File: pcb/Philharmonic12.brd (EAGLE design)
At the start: 97.8 x 95.2 mm, 47 parts, among them IC1 MC68B21, IC10 74LS74N, IC2 AY-3-8910-RP, IC3 AY-3-8910-RP, IC4 AY-3-8910-RP, IC5 AY-3-8910-RP, IC6 74LS138N, IC7 74LS30N, IC8 LM386N-1, IC9 LM386N-1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

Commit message: Small dimension updates
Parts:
- IC2, IC3, IC4, IC5: value AY-3-8910-RP -> AY-3-8910
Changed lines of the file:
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@@
 www.go4retro.com
 CC-BY-SA 4.0</text>
+<dimension x1="-25.4" y1="0" x2="-25.4" y2="95.25" x3="-55.88" y3="47.625" textsize="1.778" layer="48"/>
+<dimension x1="-48.895" y1="93.98" x2="48.895" y2="93.98" x3="0" y3="97.79" textsize="1.778" layer="48"/>
 </plain>
 <attributes>
@@
 <attribute name="VALUE" x="0" y="29.21" size="1.778" layer="27" align="bottom-center"/>
 </element>
-<element name="IC2" library="general-instrument" package="DIL40-RP" value="AY-3-8910-RP" x="-39.37" y="68.58" smashed="yes" rot="R90">
+<element name="IC2" library="general-instrument" package="DIL40-RP" value="AY-3-8910" x="-39.37" y="68.58" smashed="yes" rot="R90">
 <attribute name="NAME" x="-47.625" y="41.91" size="1.778" layer="25" ratio="10"/>
 <attribute name="VALUE" x="-38.735" y="68.58" size="1.778" layer="27" ratio="10" rot="R90" align="bottom-center"/>
 </element>
-<element name="IC3" library="general-instrument" package="DIL40-RP" value="AY-3-8910-RP" x="-21.59" y="68.58" smashed="yes" rot="R90">
+<element name="IC3" library="general-instrument" package="DIL40-RP" value="AY-3-8910" x="-21.59" y="68.58" smashed="yes" rot="R90">
 <attribute name="NAME" x="-27.305" y="40.64" size="1.778" layer="25" ratio="10"/>
 <attribute name="VALUE" x="-20.955" y="69.215" size="1.778" layer="27" ratio="10" rot="R90" align="bottom-center"/>
 </element>
-<element name="IC4" library="general-instrument" package="DIL40-RP" value="AY-3-8910-RP" x="21.59" y="68.58" smashed="yes" rot="R90">
+<element name="IC4" library="general-instrument" package="DIL40-RP" value="AY-3-8910" x="21.59" y="68.58" smashed="yes" rot="R90">
 <attribute name="NAME" x="13.97" y="40.64" size="1.778" layer="25" ratio="10"/>
 <attribute name="VALUE" x="22.225" y="68.58" size="1.778" layer="27" ratio="10" rot="R90" align="bottom-center"/>
 </element>
-<element name="IC5" library="general-instrument" package="DIL40-RP" value="AY-3-8910-RP" x="39.37" y="68.58" smashed="yes" rot="R90">
+<element name="IC5" library="general-instrument" package="DIL40-RP" value="AY-3-8910" x="39.37" y="68.58" smashed="yes" rot="R90">
 <attribute name="NAME" x="31.75" y="40.64" size="1.778" layer="25" ratio="10"/>
 <attribute name="VALUE" x="40.005" y="68.58" size="1.778" layer="27" ratio="10" rot="R90" align="bottom-center"/>

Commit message: Updates to schematic, Added BOM, and added sample code written by Chet Simpson
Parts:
- C1, C2, C3, C4: value 4m7 -> 4u7
- renumbered U$1 to CASE
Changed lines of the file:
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@@
 </autorouter>
 <elements>
-<element name="C1" library="rcl" package="E2,5-6" value="4m7" x="-6.35" y="66.04" smashed="yes" rot="R90">
+<element name="C1" library="rcl" package="E2,5-6" value="4u7" x="-6.35" y="66.04" smashed="yes" rot="R90">
 <attribute name="NAME" x="-8.89" y="63.5" size="1.016" layer="25" ratio="10" align="bottom-right"/>
 <attribute name="VALUE" x="-5.08" y="65.405" size="1.016" layer="27" ratio="10" align="bottom-right"/>
@@
 <attribute name="VALUE" x="10.16" y="64.77" size="1.016" layer="27" ratio="10"/>
 </element>
-<element name="C2" library="rcl" package="E2,5-6" value="4m7" x="6.35" y="66.04" smashed="yes" rot="R90">
+<element name="C2" library="rcl" package="E2,5-6" value="4u7" x="6.35" y="66.04" smashed="yes" rot="R90">
 <attribute name="NAME" x="8.89" y="63.5" size="1.016" layer="25" ratio="10"/>
 <attribute name="VALUE" x="5.08" y="65.405" size="1.016" layer="27" ratio="10"/>
 </element>
-<element name="C3" library="rcl" package="E2,5-6" value="4m7" x="-10.16" y="85.09" smashed="yes">
+<element name="C3" library="rcl" package="E2,5-6" value="4u7" x="-10.16" y="85.09" smashed="yes">
 <attribute name="NAME" x="-11.43" y="88.265" size="1.016" layer="25" ratio="10"/>
 <attribute name="VALUE" x="-8.89" y="82.55" size="1.016" layer="27" ratio="10" align="bottom-right"/>
 </element>
-<element name="C4" library="rcl" package="E2,5-6" value="4m7" x="10.16" y="85.09" smashed="yes" rot="R180">
+<element name="C4" library="rcl" package="E2,5-6" value="4u7" x="10.16" y="85.09" smashed="yes" rot="R180">
 <attribute name="NAME" x="9.525" y="88.265" size="1.016" layer="25" ratio="10"/>
 <attribute name="VALUE" x="8.89" y="82.55" size="1.016" layer="27" ratio="10"/>
@@
 <attribute name="VALUE" x="0" y="91.44" size="1.27" layer="27" ratio="10" align="bottom-center"/>
 </element>
-<element name="U$1" library="coco" package="PROGRAM_PAK" value="" x="0" y="42.545" smashed="yes"/>
+<element name="CASE" library="coco" package="PROGRAM_PAK" value="" x="0" y="42.545" smashed="yes"/>
 <element name="QG1" library="crystal" package="DIL08S" value="3.579545MHz" x="-40.64" y="20.32" smashed="yes">
 <attribute name="MPN" value="" x="-40.64" y="20.32" size="1.778" layer="27" display="off"/>

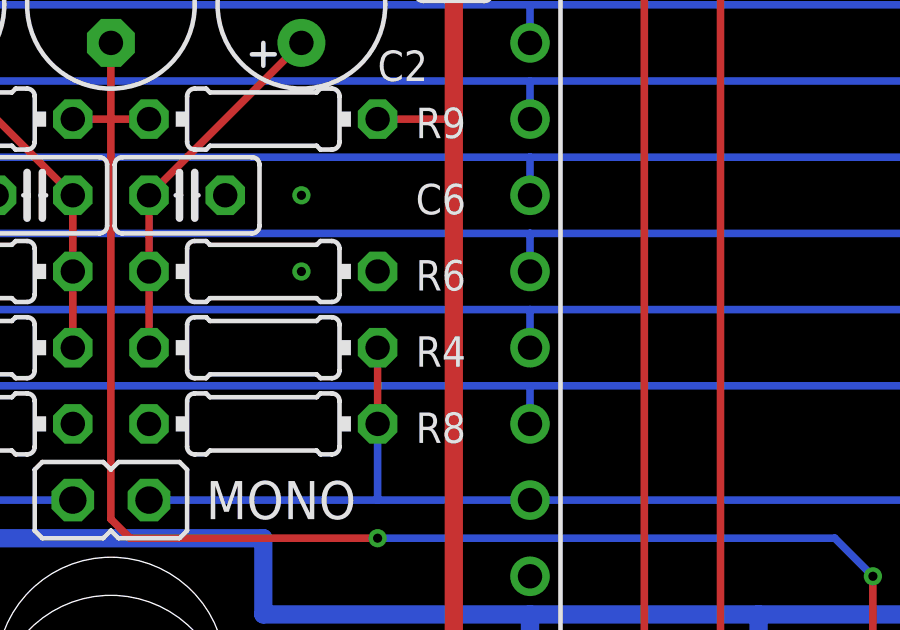
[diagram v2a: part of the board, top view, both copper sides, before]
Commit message: Fix PCB legend placement error noted in Issue #1 (hexbus reported)
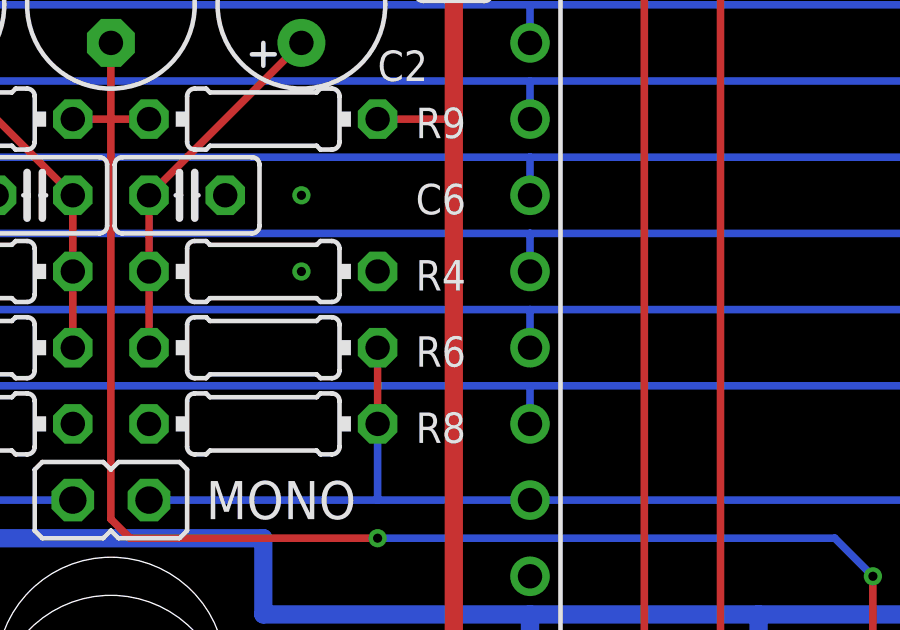
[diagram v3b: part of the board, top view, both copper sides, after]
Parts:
- C7: value 4m7 -> 4u7
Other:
- board text added: "Philharmonic 12 v1.1 PCB (c) 2018 RETRO Innovations www.go4retro.com CC-BY-SA 4.0"
- board text removed: "Philharmonic 12 PCB (c) 2018 RETRO Innovations www.go4retro.com CC-BY-SA 4.0"
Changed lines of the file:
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@@
 <wire x1="-48.895" y1="13.97" x2="-47.625" y2="12.7" width="0" layer="20" curve="90"/>
 <wire x1="-47.625" y1="12.7" x2="-26.67" y2="12.7" width="0" layer="20"/>
-<text x="0" y="12.7" size="1.4224" layer="51" ratio="10" align="bottom-center">Philharmonic 12
+<text x="0" y="12.7" size="1.4224" layer="51" ratio="10" align="bottom-center">Philharmonic 12 v1.1
 PCB (c) 2018 RETRO Innovations
 www.go4retro.com
@@
 <attribute name="VALUE" x="5.715" y="59.055" size="1.016" layer="27" ratio="10"/>
 </element>
-<element name="C7" library="rcl" package="E2,5-6" value="4m7" x="0" y="66.04" smashed="yes" rot="R270">
+<element name="C7" library="rcl" package="E2,5-6" value="4u7" x="0" y="66.04" smashed="yes" rot="R270">
 <attribute name="NAME" x="-0.635" y="69.215" size="1.016" layer="25" ratio="10"/>
 <attribute name="VALUE" x="0.127" y="65.278" size="1.016" layer="27" ratio="10" align="bottom-center"/>
@@
 </element>
 <element name="R4" library="rcl" package="0204/7" value="470" x="5.08" y="57.15" smashed="yes" rot="R180">
-<attribute name="NAME" x="10.16" y="53.975" size="1.016" layer="25" ratio="10"/>
+<attribute name="NAME" x="10.16" y="56.515" size="1.016" layer="25" ratio="10"/>
 <attribute name="VALUE" x="5.08" y="56.515" size="1.016" layer="27" ratio="10" align="bottom-center"/>
 </element>
@@
 </element>
 <element name="R6" library="rcl" package="0204/7" value="4K7" x="5.08" y="54.61" smashed="yes">
-<attribute name="NAME" x="10.16" y="56.515" size="1.016" layer="25" ratio="10"/>
+<attribute name="NAME" x="10.16" y="53.975" size="1.016" layer="25" ratio="10"/>
 <attribute name="VALUE" x="5.08" y="53.975" size="1.016" layer="27" ratio="10" align="bottom-center"/>
 </element>
